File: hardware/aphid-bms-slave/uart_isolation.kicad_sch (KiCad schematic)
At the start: 20 parts

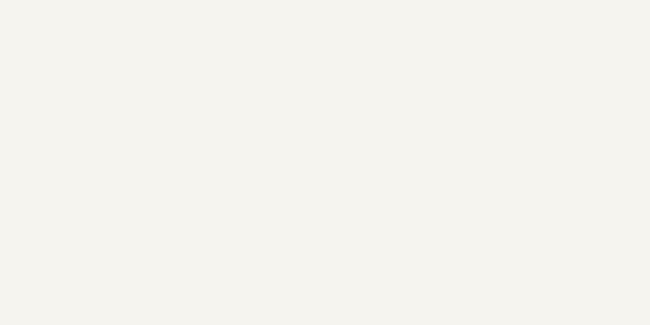
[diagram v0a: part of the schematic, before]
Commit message: Worked on BMS slave schematic
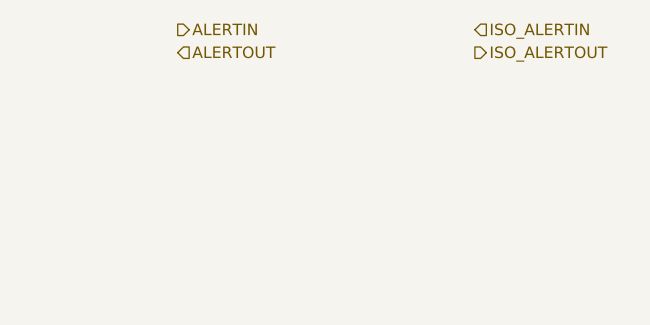
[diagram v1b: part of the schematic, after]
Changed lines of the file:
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@@
+		)
+	)
+	(hierarchical_label "ALERTIN"
+		(shape output)
+		(at 205.74 43.18 0)
+		(fields_autoplaced yes)
+		(effects
+			(font
+				(size 1.27 1.27)
+			)
+			(justify left)
+		)
+	)
+	(hierarchical_label "ISO_ALERTOUT"
+		(shape output)
+		(at 238.76 45.72 0)
+		(fields_autoplaced yes)
+		(effects
+			(font
+				(size 1.27 1.27)
+			)
+			(justify left)
 		)
 	)
@@
 		(shape input)
 		(at 137.16 151.13 0)
+		(fields_autoplaced yes)
+		(effects
+			(font
+				(size 1.27 1.27)
+			)
+			(justify left)
+		)
+	)
+	(hierarchical_label "ISO_ALERTIN"
+		(shape input)
+		(at 238.76 43.18 0)
 		(fields_autoplaced yes)
 		(effects
@@
 		)
 	)
+	(hierarchical_label "ALERTOUT"
+		(shape input)
+		(at 205.74 45.72 0)
+		(fields_autoplaced yes)
+		(effects
+			(font
+				(size 1.27 1.27)
+			)
+			(justify left)
+		)
+	)

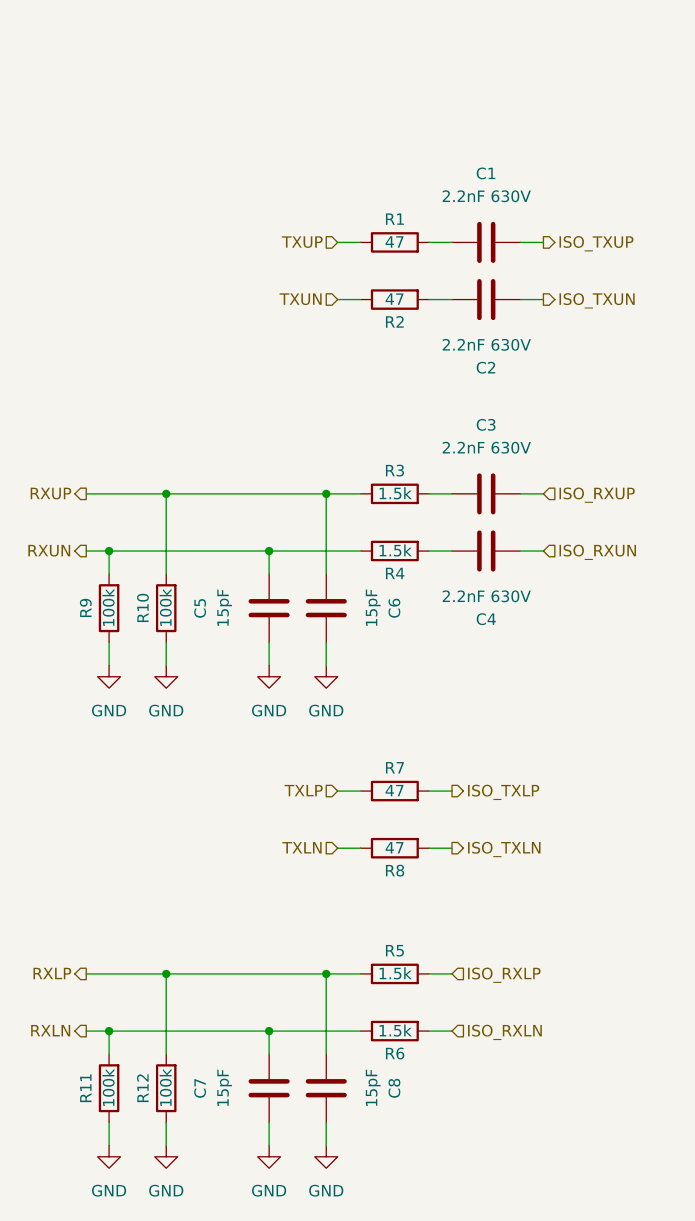
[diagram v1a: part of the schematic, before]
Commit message: Worked on BMS slave schematic and layout
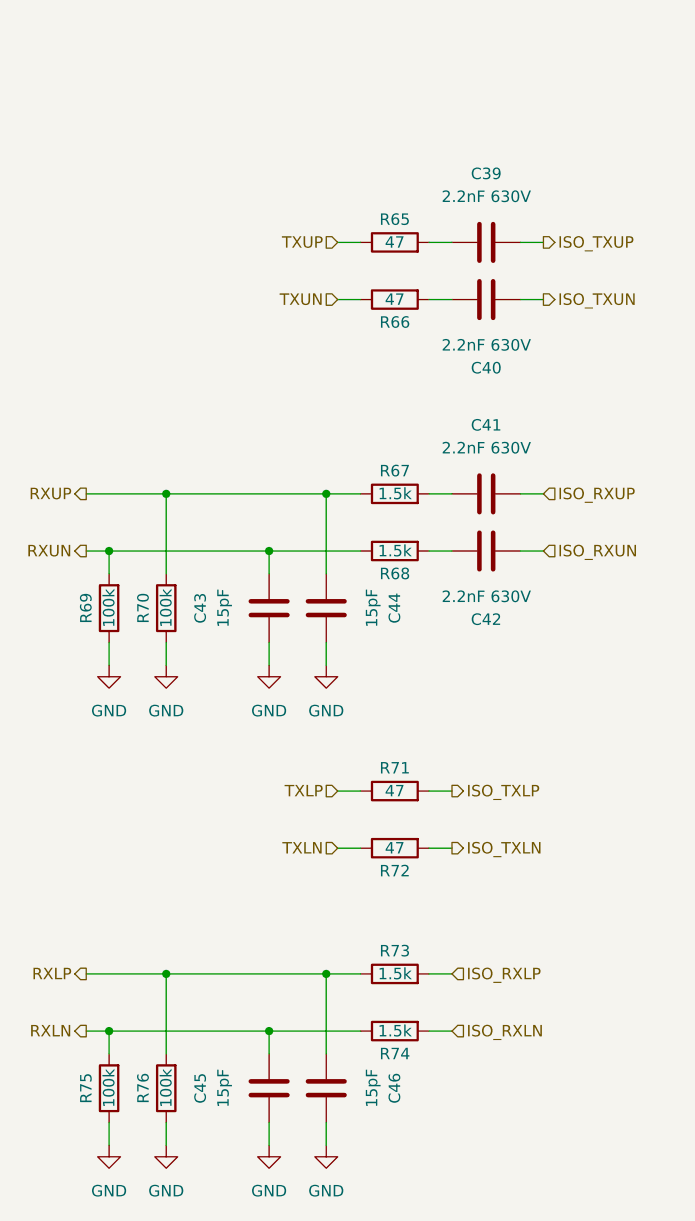
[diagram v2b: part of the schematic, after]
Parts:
- renumbered C1 to C39, C2 to C40, C3 to C41, C4 to C42, C5 to C43, C6 to C44, C7 to C45, C8 to C46, R1 to R65, R2 to R66, R3 to R67, R4 to R68, R9 to R69, R10 to R70, R7 to R71, R8 to R72, R5 to R73, R6 to R74, R11 to R75, R12 to R76
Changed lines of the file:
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@@
 		(dnp no)
 		(fields_autoplaced yes)
-		(property "Reference" "#PWR06"
+		(property "Reference" "#PWR037"
 			(at 105.41 176.53 0)
 			(effects
@@
 			(project "aphid-bms-slave"
 				(path "/36f5197f-5a2b-49d7-95ca-bb7937adb059/7420e126-c01a-46ba-a44b-0b7a6c91b65f"
-					(reference "#PWR06")
+					(reference "#PWR037")
 					(unit 1)
 				)
@@
 		(dnp no)
 		(fields_autoplaced yes)
-		(property "Reference" "#PWR02"
+		(property "Reference" "#PWR034"
 			(at 116.84 123.19 0)
 			(effects
@@
 			(project "aphid-bms-slave"
 				(path "/36f5197f-5a2b-49d7-95ca-bb7937adb059/7420e126-c01a-46ba-a44b-0b7a6c91b65f"
-					(reference "#PWR02")
+					(reference "#PWR034")
 					(unit 1)
 				)
@@
 		(on_board yes)
 		(dnp no)
-		(property "Reference" "R5"
+		(property "Reference" "R73"
 			(at 130.81 148.59 90)
 			(effects
@@
 			(project "aphid-bms-slave"
 				(path "/36f5197f-5a2b-49d7-95ca-bb7937adb059/7420e126-c01a-46ba-a44b-0b7a6c91b65f"
-					(reference "R5")
+					(reference "R73")
 					(unit 1)
 				)
@@
 		(dnp no)
 		(fields_autoplaced yes)
-		(property "Reference" "#PWR07"
+		(property "Reference" "#PWR038"
 			(at 116.84 176.53 0)
 			(effects
@@
 			(project "aphid-bms-slave"
 				(path "/36f5197f-5a2b-49d7-95ca-bb7937adb059/7420e126-c01a-46ba-a44b-0b7a6c91b65f"
-					(reference "#PWR07")
+					(reference "#PWR038")
 					(unit 1)
 				)
@@
 		(dnp no)
 		(fields_autoplaced yes)
-		(property "Reference" "#PWR03"
+		(property "Reference" "#PWR033"
 			(at 105.41 123.19 0)
 			(effects
@@
 			(project "aphid-bms-slave"
 				(path "/36f5197f-5a2b-49d7-95ca-bb7937adb059/7420e126-c01a-46ba-a44b-0b7a6c91b65f"
-					(reference "#PWR03")
+					(reference "#PWR033")
 					(unit 1)
 				)
@@
 		(on_board yes)
 		(dnp no)
-		(property "Reference" "R11"
+		(property "Reference" "R75"
 			(at 96.52 163.83 90)
 			(effects
@@
 			(project "aphid-bms-slave"
 				(path "/36f5197f-5a2b-49d7-95ca-bb7937adb059/7420e126-c01a-46ba-a44b-0b7a6c91b65f"
-					(reference "R11")
+					(reference "R75")
 					(unit 1)
 				)
@@
 		(on_board yes)
 		(dnp no)
-		(property "Reference" "R7"
+		(property "Reference" "R71"
 			(at 130.81 128.27 90)
 			(effects
@@
 			(project "aphid-bms-slave"
 				(path "/36f5197f-5a2b-49d7-95ca-bb7937adb059/7420e126-c01a-46ba-a44b-0b7a6c91b65f"
-					(reference "R7")
+					(reference "R71")
 					(unit 1)
 				)
@@
 		(on_board yes)
 		(dnp no)
-		(property "Reference" "C8"
+		(property "Reference" "C46"
 			(at 130.81 163.83 90)
 			(effects
@@
 			(project "aphid-bms-slave"
 				(path "/36f5197f-5a2b-49d7-95ca-bb7937adb059/7420e126-c01a-46ba-a44b-0b7a6c91b65f"
-					(reference "C8")
+					(reference "C46")
 					(unit 1)
 				)
@@
 		(dnp no)
 		(fields_autoplaced yes)
-		(property "Reference" "#PWR05"
+		(property "Reference" "#PWR036"
 			(at 99.06 176.53 0)
 			(effects
@@
 			(project "aphid-bms-slave"
 				(path "/36f5197f-5a2b-49d7-95ca-bb7937adb059/7420e126-c01a-46ba-a44b-0b7a6c91b65f"
-					(reference "#PWR05")
+					(reference "#PWR036")
 					(unit 1)
 				)
@@
 		(on_board yes)
 		(dnp no)
-		(property "Reference" "R4"
+		(property "Reference" "R68"
 			(at 130.81 106.68 90)
 			(effects
@@
 			(project "aphid-bms-slave"
 				(path "/36f5197f-5a2b-49d7-95ca-bb7937adb059/7420e126-c01a-46ba-a44b-0b7a6c91b65f"
-					(reference "R4")
+					(reference "R68")
 					(unit 1)
 				)
@@
 		(dnp no)
 		(fields_autoplaced yes)
-		(property "Reference" "#PWR08"
+		(property "Reference" "#PWR039"
 			(at 123.19 176.53 0)
 			(effects
@@
 			(project "aphid-bms-slave"
 				(path "/36f5197f-5a2b-49d7-95ca-bb7937adb059/7420e126-c01a-46ba-a44b-0b7a6c91b65f"
-					(reference "#PWR08")
+					(reference "#PWR039")
 					(unit 1)
 				)
@@
 		(dnp no)
 		(fields_autoplaced yes)
-		(property "Reference" "#PWR04"
+		(property "Reference" "#PWR032"
 			(at 99.06 123.19 0)
 			(effects
@@
 			(project "aphid-bms-slave"
 				(path "/36f5197f-5a2b-49d7-95ca-bb7937adb059/7420e126-c01a-46ba-a44b-0b7a6c91b65f"
-					(reference "#PWR04")
+					(reference "#PWR032")
 					(unit 1)
 				)
@@
 		(on_board yes)
 		(dnp no)
-		(property "Reference" "R3"
+		(property "Reference" "R67"
 			(at 130.81 95.25 90)
 			(effects
@@
 			(project "aphid-bms-slave"
 				(path "/36f5197f-5a2b-49d7-95ca-bb7937adb059/7420e126-c01a-46ba-a44b-0b7a6c91b65f"
-					(reference "R3")
+					(reference "R67")
 					(unit 1)
 				)
@@
 		(dnp no)
 		(fields_autoplaced yes)
-		(property "Reference" "#PWR01"
+		(property "Reference" "#PWR035"
 			(at 123.19 123.19 0)
 			(effects
@@
 			(project ""
 				(path "/36f5197f-5a2b-49d7-95ca-bb7937adb059/7420e126-c01a-46ba-a44b-0b7a6c91b65f"
-					(reference "#PWR01")
+					(reference "#PWR035")
 					(unit 1)
 				)
@@
 		(on_board yes)
 		(dnp no)
-		(property "Reference" "R2"
+		(property "Reference" "R66"
 			(at 130.81 78.74 90)
 			(effects
@@
 			(project "aphid-bms-slave"
 				(path "/36f5197f-5a2b-49d7-95ca-bb7937adb059/7420e126-c01a-46ba-a44b-0b7a6c91b65f"
-					(reference "R2")
+					(reference "R66")
 					(unit 1)
 				)
@@
 		(on_board yes)
 		(dnp no)
-		(property "Reference" "C7"
+		(property "Reference" "C45"
 			(at 109.22 163.83 90)
 			(effects
@@
 			(project "aphid-bms-slave"
 				(path "/36f5197f-5a2b-49d7-95ca-bb7937adb059/7420e126-c01a-46ba-a44b-0b7a6c91b65f"
-					(reference "C7")
+					(reference "C45")
 					(unit 1)
 				)
@@
 		(on_board yes)
 		(dnp no)
-		(property "Reference" "R10"
+		(property "Reference" "R70"
 			(at 102.87 110.49 90)
 			(effects
@@
 			(project "aphid-bms-slave"
 				(path "/36f5197f-5a2b-49d7-95ca-bb7937adb059/7420e126-c01a-46ba-a44b-0b7a6c91b65f"
-					(reference "R10")
+					(reference "R70")
 					(unit 1)
 				)
@@
 		(on_board yes)
 		(dnp no)
-		(property "Reference" "C6"
+		(property "Reference" "C44"
 			(at 130.81 110.49 90)
 			(effects
@@
 			(project "aphid-bms-slave"
 				(path "/36f5197f-5a2b-49d7-95ca-bb7937adb059/7420e126-c01a-46ba-a44b-0b7a6c91b65f"
-					(reference "C6")
+					(reference "C44")
 					(unit 1)
 				)
@@
 		(on_board yes)
 		(dnp no)
-		(property "Reference" "C2"
+		(property "Reference" "C40"
 			(at 140.97 83.82 90)
 			(effects
@@
 			(project "aphid-bms-slave"
 				(path "/36f5197f-5a2b-49d7-95ca-bb7937adb059/7420e126-c01a-46ba-a44b-0b7a6c91b65f"
-					(reference "C2")
+					(reference "C40")
 					(unit 1)
 				)
@@
 		(on_board yes)
 		(dnp no)
-		(property "Reference" "R9"
+		(property "Reference" "R69"
 			(at 96.52 110.49 90)
 			(effects
@@
 			(project "aphid-bms-slave"
 				(path "/36f5197f-5a2b-49d7-95ca-bb7937adb059/7420e126-c01a-46ba-a44b-0b7a6c91b65f"
-					(reference "R9")
+					(reference "R69")
 					(unit 1)
 				)
@@
 		(on_board yes)
 		(dnp no)
-		(property "Reference" "C5"
+		(property "Reference" "C43"
 			(at 109.22 110.49 90)
 			(effects
@@
 			(project "aphid-bms-slave"
 				(path "/36f5197f-5a2b-49d7-95ca-bb7937adb059/7420e126-c01a-46ba-a44b-0b7a6c91b65f"
-					(reference "C5")
+					(reference "C43")
 					(unit 1)
 				)
@@
 		(on_board yes)
 		(dnp no)
-		(property "Reference" "R8"
+		(property "Reference" "R72"
 			(at 130.81 139.7 90)
 			(effects
@@
 			(project "aphid-bms-slave"
 				(path "/36f5197f-5a2b-49d7-95ca-bb7937adb059/7420e126-c01a-46ba-a44b-0b7a6c91b65f"
-					(reference "R8")
+					(reference "R72")
 					(unit 1)
 				)
@@
 		(dnp no)
 		(fields_autoplaced yes)
-		(property "Reference" "C3"
+		(property "Reference" "C41"
 			(at 140.97 90.17 90)
 			(effects
@@
 			(project "aphid-bms-slave"
 				(path "/36f5197f-5a2b-49d7-95ca-bb7937adb059/7420e126-c01a-46ba-a44b-0b7a6c91b65f"
-					(reference "C3")
+					(reference "C41")
 					(unit 1)
 				)
@@
 		(dnp no)
 		(fields_autoplaced yes)
-		(property "Reference" "C1"
+		(property "Reference" "C39"
 			(at 140.97 62.23 90)
 			(effects
@@
 			(project ""
 				(path "/36f5197f-5a2b-49d7-95ca-bb7937adb059/7420e126-c01a-46ba-a44b-0b7a6c91b65f"
-					(reference "C1")
+					(reference "C39")
 					(unit 1)
 				)
@@
 		(on_board yes)
 		(dnp no)
-		(property "Reference" "R6"
+		(property "Reference" "R74"
 			(at 130.81 160.02 90)
 			(effects
@@
 			(project "aphid-bms-slave"
 				(path "/36f5197f-5a2b-49d7-95ca-bb7937adb059/7420e126-c01a-46ba-a44b-0b7a6c91b65f"
-					(reference "R6")
+					(reference "R74")
 					(unit 1)
 				)
@@
 		(on_board yes)
 		(dnp no)
-		(property "Reference" "R1"
+		(property "Reference" "R65"
 			(at 130.81 67.31 90)
 			(effects
@@
 			(project ""
 				(path "/36f5197f-5a2b-49d7-95ca-bb7937adb059/7420e126-c01a-46ba-a44b-0b7a6c91b65f"
-					(reference "R1")
+					(reference "R65")
 					(unit 1)
 				)
@@
 		(on_board yes)
 		(dnp no)
-		(property "Reference" "C4"
+		(property "Reference" "C42"
 			(at 140.97 111.76 90)
 			(effects
@@
 			(project "aphid-bms-slave"
 				(path "/36f5197f-5a2b-49d7-95ca-bb7937adb059/7420e126-c01a-46ba-a44b-0b7a6c91b65f"
-					(reference "C4")
+					(reference "C42")
 					(unit 1)
 				)
@@
 		(on_board yes)
 		(dnp no)
-		(property "Reference" "R12"
+		(property "Reference" "R76"
 			(at 102.87 163.83 90)
 			(effects
@@
 			(project "aphid-bms-slave"
 				(path "/36f5197f-5a2b-49d7-95ca-bb7937adb059/7420e126-c01a-46ba-a44b-0b7a6c91b65f"
-					(reference "R12")
-					(unit 1)
-				)
+					(reference "R76")
+					(unit 1)
+				)

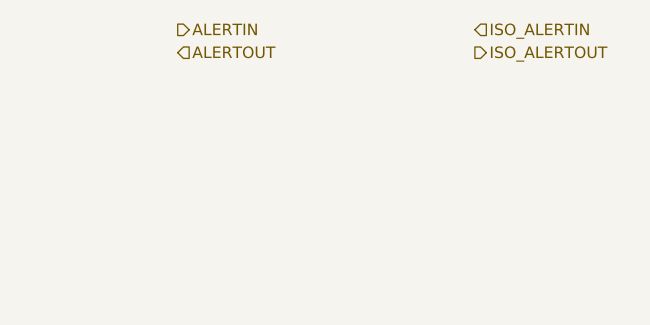
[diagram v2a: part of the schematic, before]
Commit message: Worked on BMS slave schematic and layout
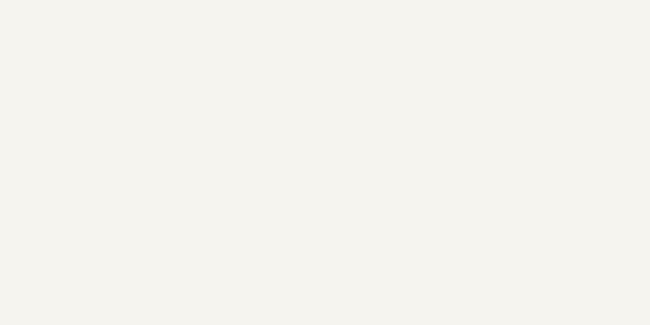
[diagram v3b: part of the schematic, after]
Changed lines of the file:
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@@
-		)
-	)
-	(hierarchical_label "ALERTIN"
-		(shape output)
-		(at 205.74 43.18 0)
-		(fields_autoplaced yes)
-		(effects
-			(font
-				(size 1.27 1.27)
-			)
-			(justify left)
-		)
-	)
-	(hierarchical_label "ISO_ALERTOUT"
-		(shape output)
-		(at 238.76 45.72 0)
-		(fields_autoplaced yes)
-		(effects
-			(font
-				(size 1.27 1.27)
-			)
-			(justify left)
 		)
 	)
@@
 		(shape input)
 		(at 137.16 151.13 0)
-		(fields_autoplaced yes)
-		(effects
-			(font
-				(size 1.27 1.27)
-			)
-			(justify left)
-		)
-	)
-	(hierarchical_label "ISO_ALERTIN"
-		(shape input)
-		(at 238.76 43.18 0)
 		(fields_autoplaced yes)
 		(effects
@@
 		)
 	)
-	(hierarchical_label "ALERTOUT"
-		(shape input)
-		(at 205.74 45.72 0)
-		(fields_autoplaced yes)
-		(effects
-			(font
-				(size 1.27 1.27)
-			)
-			(justify left)
-		)
-	)

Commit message: BMS slave 1.0 done
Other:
- company: (none) -> https://aphid-ev.se
- title: (none) -> aphid-ev BMS slave
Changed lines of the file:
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@@
 	(generator_version "8.0")
 	(paper "A4")
+	(title_block
+		(title "aphid-ev BMS slave")
+		(date "2024-07-23")
+		(rev "1.0")
+		(company "https://aphid-ev.se")
+	)
 	(junction
 		(at 99.06 104.14)
